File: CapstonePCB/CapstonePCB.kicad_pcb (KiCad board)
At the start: 2 copper layers, 42 parts, among them J1 Conn_02x40_Counter_Clockwise, J2 Barrel_Jack, SW1 SW_Push, SW2 SW_Push, SW3 SW_Push, U1 NUCLEO64-F411RE, U2 LP-MSPM0G3507, U3 STSPIN220, U4 SN74AHC14N, U5 LM7805_TO220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

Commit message: Formatting
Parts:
- moved C_EN1 58.1 mm to (194.6, 93.2)
- moved R_COFF1 58.1 mm to (199.0, 91.5)
- moved R_OFF1 58.1 mm to (199.0, 93.2)
- moved R_SNSA1 58.1 mm to (188.9, 82.1)
- moved R_SNSB1 58.1 mm to (196.8, 87.8)
- moved R_STBY1 58.1 mm to (199.0, 78.0)
- moved U3 58.1 mm to (192.8, 84.9)
- moved C_STBY1 58.1 mm to (191.7, 80.5)
- moved R_EN1 58.1 mm to (193.9, 80.5)
- moved C_EN2 58.1 mm to (191.4, 78.0)
- moved C_SPOIL1 58.1 mm to (191.7, 90.7)
- moved C_s1 58.1 mm to (194.3, 88.2)
- moved PullUpResistor2 10.2 mm to (160.0, 104.5), turned to -90 degrees
- moved C3 7.29 mm to (193.0, 27.9)
- moved C_STBY3 2.54 mm to (33.0, 22.8)
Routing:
- net GNDREF: track 189.5 -> 269.6 mm
- net +12V: track 21.0 -> 23.2 mm
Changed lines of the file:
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@@
 	(footprint "Resistor_SMD:R_0201_0603Metric"
 		(layer "F.Cu")
-		(at 243.495 54.13)
+		(at 199.0125 91.4925)
 		(descr "Resistor SMD 0201 (0603 Metric), square (rectangular) end terminal, IPC-7351 nominal, (Body size source: https://www.vishay.com/docs/20052/crcw0201e3.pdf), generated with kicad-footprint-generator")
 		(tags "resistor")
@@
 	(footprint "Capacitor_SMD:C_0201_0603Metric"
 		(layer "F.Cu")
-		(at 235.875 40.64)
+		(at 191.3925 78.0025)
 		(descr "Capacitor SMD 0201 (0603 Metric), square (rectangular) end terminal, IPC-7351 nominal, (Body size source: https://www.vishay.com/docs/20052/crcw0201e3.pdf), generated with kicad-footprint-generator")
 		(tags "capacitor")
@@
 	(footprint "Capacitor_SMD:C_0201_0603Metric"
 		(layer "F.Cu")
-		(at 236.22 43.18)
+		(at 191.7375 80.5425)
 		(descr "Capacitor SMD 0201 (0603 Metric), square (rectangular) end terminal, IPC-7351 nominal, (Body size source: https://www.vishay.com/docs/20052/crcw0201e3.pdf), generated with kicad-footprint-generator")
 		(tags "capacitor")
@@
 	(footprint "Capacitor_SMD:C_0201_0603Metric"
 		(layer "F.Cu")
-		(at 236.22 53.34)
+		(at 191.7375 90.7025)
 		(descr "Capacitor SMD 0201 (0603 Metric), square (rectangular) end terminal, IPC-7351 nominal, (Body size source: https://www.vishay.com/docs/20052/crcw0201e3.pdf), generated with kicad-footprint-generator")
 		(tags "capacitor")
@@
 	(footprint "Resistor_SMD:R_0201_0603Metric"
 		(layer "F.Cu")
-		(at 169.835 101.6)
+		(at 160.02 104.46 -90)
 		(descr "Resistor SMD 0201 (0603 Metric), square (rectangular) end terminal, IPC-7351 nominal, (Body size source: https://www.vishay.com/docs/20052/crcw0201e3.pdf), generated with kicad-footprint-generator")
 		(tags "resistor")
 		(property "Reference" "PullUpResistor2"
-			(at 0 -1.05 0)
+			(at 0 -1.05 90)
 			(layer "F.SilkS")
 			(effects
@@
 		)
 		(property "Value" "10 kOhm"
-			(at 0 1.05 0)
+			(at 0 1.05 90)
 			(layer "F.Fab")
 			(effects
@@
 		)
 		(property "Datasheet" "~"
-			(at 0 0 0)
+			(at 0 0 90)
 			(layer "F.Fab")
 			(hide yes)
@@
 		)
 		(property "Description" "Resistor"
-			(at 0 0 0)
+			(at 0 0 90)
 			(layer "F.Fab")
 			(hide yes)
@@
 		(attr smd)
 		(fp_line
-			(start -0.7 -0.35)
-			(end 0.7 -0.35)
+			(start -0.7 0.35)
+			(end -0.7 -0.35)
 			(stroke
 				(width 0.05)
@@
 		)
 		(fp_line
-			(start -0.7 0.35)
-			(end -0.7 -0.35)
+			(start 0.7 0.35)
+			(end -0.7 0.35)
 			(stroke
 				(width 0.05)
@@
 		)
 		(fp_line
-			(start 0.7 -0.35)
-			(end 0.7 0.35)
+			(start -0.7 -0.35)
+			(end 0.7 -0.35)
 			(stroke
 				(width 0.05)
@@
 		)
 		(fp_line
-			(start 0.7 0.35)
-			(end -0.7 0.35)
+			(start 0.7 -0.35)
+			(end 0.7 0.35)
 			(stroke
 				(width 0.05)
@@
 		)
 		(fp_line
-			(start -0.3 -0.15)
-			(end 0.3 -0.15)
+			(start -0.3 0.15)
+			(end -0.3 -0.15)
 			(stroke
 				(width 0.1)
@@
 		)
 		(fp_line
-			(start -0.3 0.15)
-			(end -0.3 -0.15)
+			(start 0.3 0.15)
+			(end -0.3 0.15)
 			(stroke
 				(width 0.1)
@@
 		)
 		(fp_line
-			(start 0.3 -0.15)
-			(end 0.3 0.15)
+			(start -0.3 -0.15)
+			(end 0.3 -0.15)
 			(stroke
 				(width 0.1)
@@
 		)
 		(fp_line
-			(start 0.3 0.15)
-			(end -0.3 0.15)
+			(start 0.3 -0.15)
+			(end 0.3 0.15)
 			(stroke
 				(width 0.1)
@@
 		)
 		(fp_text user "${REFERENCE}"
-			(at 0 -0.68 0)
+			(at 0 -0.68 90)
 			(layer "F.Fab")
 			(effects
@@
 		)
 		(pad "" smd roundrect
-			(at -0.345 0)
+			(at -0.345 0 270)
 			(size 0.318 0.36)
 			(layers "F.Paste")
@@
 		)
 		(pad "" smd roundrect
-			(at 0.345 0)
+			(at 0.345 0 270)
 			(size 0.318 0.36)
 			(layers "F.Paste")
@@
 		)
 		(pad "1" smd roundrect
-			(at -0.32 0)
+			(at -0.32 0 270)
 			(size 0.46 0.4)
 			(layers "F.Cu" "F.Mask")
@@
 		)
 		(pad "2" smd roundrect
-			(at 0.32 0)
+			(at 0.32 0 270)
 			(size 0.46 0.4)
 			(layers "F.Cu" "F.Mask")
@@
 	(footprint "Resistor_SMD:R_0201_0603Metric"
 		(layer "F.Cu")
-		(at 241.3 50.48 -90)
+		(at 196.8175 87.8425 -90)
 		(descr "Resistor SMD 0201 (0603 Metric), square (rectangular) end terminal, IPC-7351 nominal, (Body size source: https://www.vishay.com/docs/20052/crcw0201e3.pdf), generated with kicad-footprint-generator")
 		(tags "resistor")
@@
 	(footprint "Resistor_SMD:R_0201_0603Metric"
 		(layer "F.Cu")
-		(at 243.495 55.88)
+		(at 199.0125 93.2425)
 		(descr "Resistor SMD 0201 (0603 Metric), square (rectangular) end terminal, IPC-7351 nominal, (Body size source: https://www.vishay.com/docs/20052/crcw0201e3.pdf), generated with kicad-footprint-generator")
 		(tags "resistor")
@@
 	(footprint "Capacitor_THT:C_Radial_D10.0mm_H20.0mm_P5.00mm"
 		(layer "F.Cu")
-		(at 30.48 22.78 90)
+		(at 33.02 22.78 90)
 		(descr "C, Radial series, Radial, pin pitch=5.00mm, diameter=10mm, height=20mm, Non-Polar Electrolytic Capacitor")
 		(tags "C Radial series Radial pin pitch 5.00mm diameter 10mm height 20mm Non-Polar Electrolytic Capacitor")
@@
 	(footprint "Capacitor_SMD:C_0201_0603Metric"
 		(layer "F.Cu")
-		(at 238.76 50.8)
+		(at 194.2775 88.1625)
 		(descr "Capacitor SMD 0201 (0603 Metric), square (rectangular) end terminal, IPC-7351 nominal, (Body size source: https://www.vishay.com/docs/20052/crcw0201e3.pdf), generated with kicad-footprint-generator")
 		(tags "capacitor")
@@
 	(footprint "Package_DFN_QFN:VQFN-16-1EP_3x3mm_P0.5mm_EP1.8x1.8mm"
 		(layer "F.Cu")
-		(at 237.2725 47.51)
+		(at 192.79 84.8725)
 		(descr "VQFN, 16 Pin (https://www.st.com/resource/en/datasheet/stspin220.pdf), generated with kicad-footprint-generator ipc_noLead_generator.py")
 		(tags "VQFN NoLead")
@@
 	(footprint "Capacitor_SMD:C_0201_0603Metric"
 		(layer "F.Cu")
-		(at 192.695 35.22)
+		(at 193.04 27.94)
 		(descr "Capacitor SMD 0201 (0603 Metric), square (rectangular) end terminal, IPC-7351 nominal, (Body size source: https://www.vishay.com/docs/20052/crcw0201e3.pdf), generated with kicad-footprint-generator")
 		(tags "capacitor")
@@
 	(footprint "Capacitor_SMD:C_0201_0603Metric"
 		(layer "F.Cu")
-		(at 239.08 55.88 180)
+		(at 194.5975 93.2425 180)
 		(descr "Capacitor SMD 0201 (0603 Metric), square (rectangular) end terminal, IPC-7351 nominal, (Body size source: https://www.vishay.com/docs/20052/crcw0201e3.pdf), generated with kicad-footprint-generator")
 		(tags "capacitor")
@@
 	(footprint "Resistor_SMD:R_0201_0603Metric"
 		(layer "F.Cu")
-		(at 233.335 44.76)
+		(at 188.8525 82.1225)
 		(descr "Resistor SMD 0201 (0603 Metric), square (rectangular) end terminal, IPC-7351 nominal, (Body size source: https://www.vishay.com/docs/20052/crcw0201e3.pdf), generated with kicad-footprint-generator")
 		(tags "resistor")
@@
 	(footprint "Resistor_SMD:R_0201_0603Metric"
 		(layer "F.Cu")
-		(at 243.495 40.64)
+		(at 199.0125 78.0025)
 		(descr "Resistor SMD 0201 (0603 Metric), square (rectangular) end terminal, IPC-7351 nominal, (Body size source: https://www.vishay.com/docs/20052/crcw0201e3.pdf), generated with kicad-footprint-generator")
 		(tags "resistor")
@@
 	(footprint "Resistor_SMD:R_0201_0603Metric"
 		(layer "F.Cu")
-		(at 238.415 43.18)
+		(at 193.9325 80.5425)
 		(descr "Resistor SMD 0201 (0603 Metric), square (rectangular) end terminal, IPC-7351 nominal, (Body size source: https://www.vishay.com/docs/20052/crcw0201e3.pdf), generated with kicad-footprint-generator")
 		(tags "resistor")
@@
 	)
 	(segment
-		(start 30.48 24.45)
-		(end 34.895 28.865)
+		(start 27.94 26.99)
+		(end 28.81 26.99)
+		(width 0.25)
+		(layer "F.Cu")
+		(net 168)
+	)
+	(segment
+		(start 33.02 22.78)
+		(end 33.02 26.99)
 		(width 0.25)
 		(layer "F.Cu")
@@
 	)
 	(segment
-		(start 30.48 24.45)
-		(end 27.94 26.99)
+		(start 28.81 26.99)
+		(end 33.02 22.78)
 		(width 0.25)
 		(layer "F.Cu")
@@
 	)
 	(segment
-		(start 30.48 22.78)
-		(end 30.48 24.45)
+		(start 34.895 28.865)
+		(end 34.895 30.48)
 		(width 0.25)
 		(layer "F.Cu")
@@
 	)
 	(segment
-		(start 34.895 28.865)
-		(end 34.895 30.48)
+		(start 33.02 26.99)
+		(end 34.895 28.865)
 		(width 0.25)
 		(layer "F.Cu")
@@
 	)
 	(segment
+		(start 147.020884 94.074)
+		(end 154.034 94.074)
+		(width 0.25)
+		(layer "F.Cu")
+		(net 169)
+	)
+	(segment
 		(start 22.86 33.97)
 		(end 22.86 38.1)
@@
 	)
 	(segment
+		(start 145.562884 92.616)
+		(end 147.020884 94.074)
+		(width 0.25)
+		(layer "F.Cu")
+		(net 169)
+	)
+	(segment
 		(start 84.906 143.326)
 		(end 83.82 142.24)
@@
 	)
 	(segment
+		(start 22.86 17.78)
+		(end 33.02 17.78)
+		(width 0.25)
+		(layer "F.Cu")
+		(net 169)
+	)
+	(segment
+		(start 87.536 92.616)
+		(end 145.562884 92.616)
+		(width 0.25)
+		(layer "F.Cu")
+		(net 169)
+	)
+	(segment
 		(start 35.56 35.56)
 		(end 35.56 39.951116)
@@
 	)
 	(segment
+		(start 87.446 92.526)
+		(end 87.536 92.616)
+		(width 0.25)
+		(layer "F.Cu")
+		(net 169)
+	)
+	(segment
 		(start 28.89 28.89)
 		(end 35.56 35.56)
@@
 	)
 	(segment
+		(start 156.77 96.81)
+		(end 163.27 96.81)
+		(width 0.25)
+		(layer "F.Cu")
+		(net 169)
+	)
+	(segment
 		(start 20.32 20.32)
 		(end 17.696 22.944)
@@
 	)
 	(segment
-		(start 30.48 17.78)
-		(end 22.86 17.78)
-		(width 0.25)
-		(layer "F.Cu")
-		(net 169)
-	)
-	(segment
 		(start 46.207116 49.624)
 		(end 46.896 50.312884)
@@
 		(width 0.25)
 		(layer "F.Cu")
+		(net 169)
+	)
+	(segment
+		(start 154.034 94.074)
+		(end 156.77 96.81)
+		(width 0.25)
+		(layer "F.Cu")

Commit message: Updated button routing
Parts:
- CSW1: renamed from C1; value 0.47 uF -> 0.47uF
- CSW3: renamed from C2; value 0.47 uF -> 0.47uF
- PullUpResistorSW1: renamed from PullUpResistor1; value 10 kOhm -> 10kOhm
- PullUpResistorSW3: renamed from PullUpResistor3; value 10 kOhm -> 10kOhm
- RSW1: renamed from R1; value 10 kOhm -> 10kOhm
- moved U7 86.1 mm to (256.5, 69.5)
- moved PullUpResistorJS1 54.3 mm to (246.0, 50.8)
- moved CJS1 51.1 mm to (235.9, 55.9)
- moved RJS1 43.4 mm to (235.9, 48.3)
- moved PullUpResistorSW3 30.1 mm to (221.7, 30.8)
- moved RSW3 12.2 mm to (201.0, 33.3)
- moved SW1 11.4 mm to (205.0, 18.1)
- moved CSW3 10.5 mm to (201.1, 28.2)
- moved SW3 10.5 mm to (207.6, 28.2)
- moved CSW1 10.2 mm to (200.7, 17.8)
- moved RSW1 7.83 mm to (200.3, 22.9), turned to 0 degrees
- moved PullUpResistorSW1 7.43 mm to (218.4, 20.0)
- renumbered C3 to CJS1, PullUpResistor4 to PullUpResistorJS1, R3 to RJS1, R2 to RSW3
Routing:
- net +5V: track 136.0 -> 324.0 mm
- net GNDREF: track 269.6 -> 358.7 mm
- net Net-(J1-Pin_5): track 2.54 -> 36.4 mm
- net Net-(J1-Pin_3): track 2.54 -> 35.3 mm
- net Net-(J1-Pin_1): track 2.54 -> 34.3 mm
- net Net-(U4-2A): track 0.00 -> 28.0 mm
- net Net-(U4-1A): track 0.00 -> 25.5 mm
- net VDD: track 243.0 -> 219.3 mm
- net /Button2 Input: track 0.00 -> 21.1 mm
- net /Button1 Input: track 0.00 -> 18.9 mm
- net /Button No Debouning: track 2.54 -> 18.7 mm

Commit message: Updated rounting
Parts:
- renumbered C_STBY2 to C_BP1, C_STBY3 to C_BP2
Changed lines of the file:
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@@
 		(descr "Capacitor SMD 0805 (2012 Metric), square (rectangular) end terminal, IPC-7351 nominal, (Body size source: IPC-SM-782 page 76, https://www.pcb-3d.com/wordpress/wp-content/uploads/ipc-sm-782a_amendment_1_and_2.pdf, https://docs.google.com/spreadsheets/d/1BsfQQcO9C6DZCsRaXUlFlo91Tg2WpOkGARC1WS5S8t0/edit?usp=sharing), generated with kicad-footprint-generator")
 		(tags "capacitor")
-		(property "Reference" "C_STBY2"
+		(property "Reference" "C_BP1"
 			(at 0 -1.68 90)
 			(layer "F.SilkS")
@@
 		(descr "C, Radial series, Radial, pin pitch=5.00mm, diameter=10mm, height=20mm, Non-Polar Electrolytic Capacitor")
 		(tags "C Radial series Radial pin pitch 5.00mm diameter 10mm height 20mm Non-Polar Electrolytic Capacitor")
-		(property "Reference" "C_STBY3"
+		(property "Reference" "C_BP2"
 			(at 2.5 -6.25 90)
 			(layer "F.SilkS")

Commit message: Formatting change
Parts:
- moved U8 1.95 mm to (165.1, 114.3)
- renumbered R_STBY2 to R_INDC1
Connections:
- J1 pad 27: GNDREF -> Net-(J1-Pin_27)
- J1 pad 28: GNDREF -> Net-(J1-Pin_27)
- U3 pad 11: GNDREF -> unconnected-(U3-REF-Pad11)
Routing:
- net GNDREF: track 358.7 -> 27.2 mm
- net +5V: track 324.0 -> 287.4 mm
- net VDD: track 219.3 -> 196.9 mm
- net Net-(J1-Pin_79): track 2.54 -> 21.3 mm
- net Net-(J1-Pin_77): track 2.54 -> 21.1 mm
- net +12V: track 23.2 -> 35.0 mm
- net Net-(J1-Pin_27): track 0.00 -> 2.54 mm

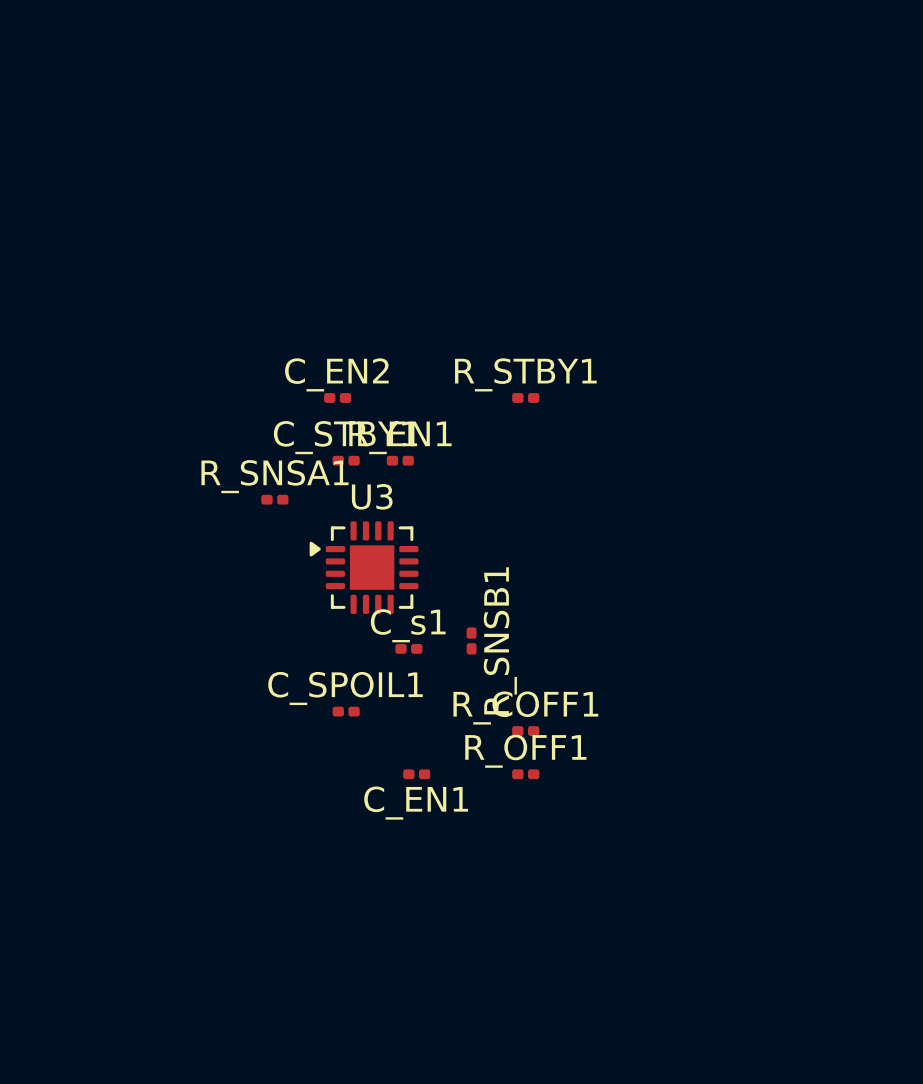
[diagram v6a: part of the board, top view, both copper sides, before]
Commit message: Changed caps to through-hole
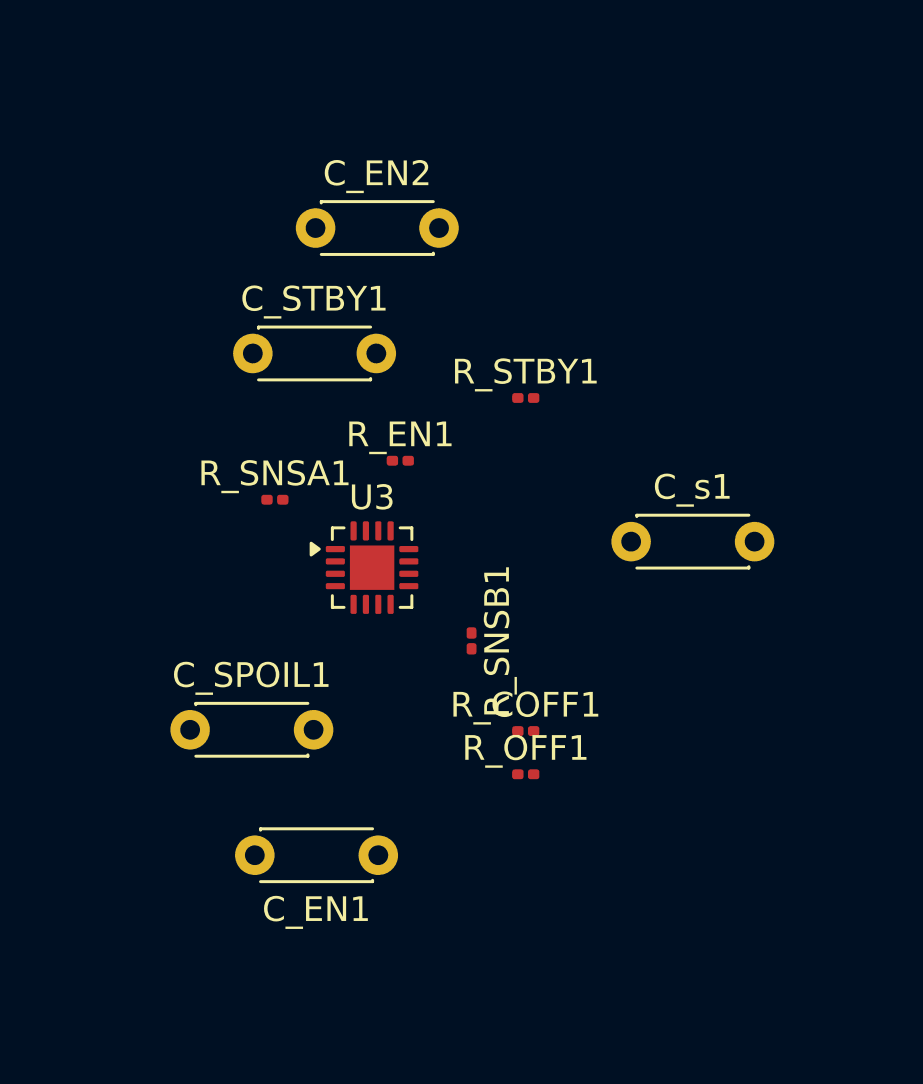
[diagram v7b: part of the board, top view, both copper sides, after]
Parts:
- C_EN1, C_EN2, C_SPOIL1, C_STBY1, C_s1: footprint Capacitor_SMD:C_0201_0603Metric -> Capacitor_THT:C_Disc_D4.3mm_W1.9mm_P5.00mm
- moved C_s1 10.00 mm to (203.3, 83.8)
- moved C_EN2 6.94 mm to (190.5, 71.1)
- moved C_SPOIL1 6.36 mm to (185.4, 91.4)
- moved C_STBY1 5.76 mm to (188.0, 76.2)
- moved C_EN1 3.63 mm to (193.0, 96.5)
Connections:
- U3 pad 11: unconnected-(U3-REF-Pad11) -> Net-(J1-Pin_27)
- U7 pad H2: Net-(J1-Pin_21) -> Net-(J1-Pin_11)
- U7 pad V2: Net-(J1-Pin_23) -> Net-(J1-Pin_13)

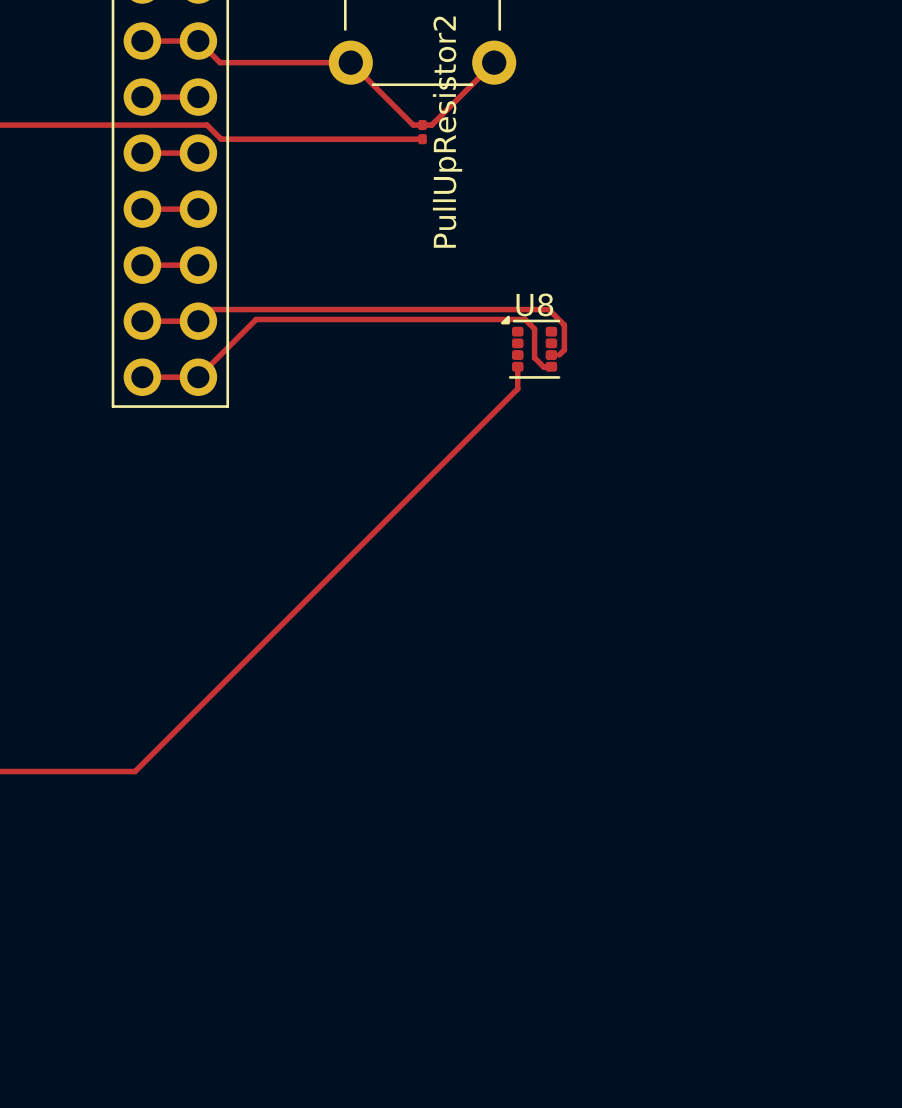
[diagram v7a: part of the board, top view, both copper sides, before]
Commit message: Added LCD connector to schematic
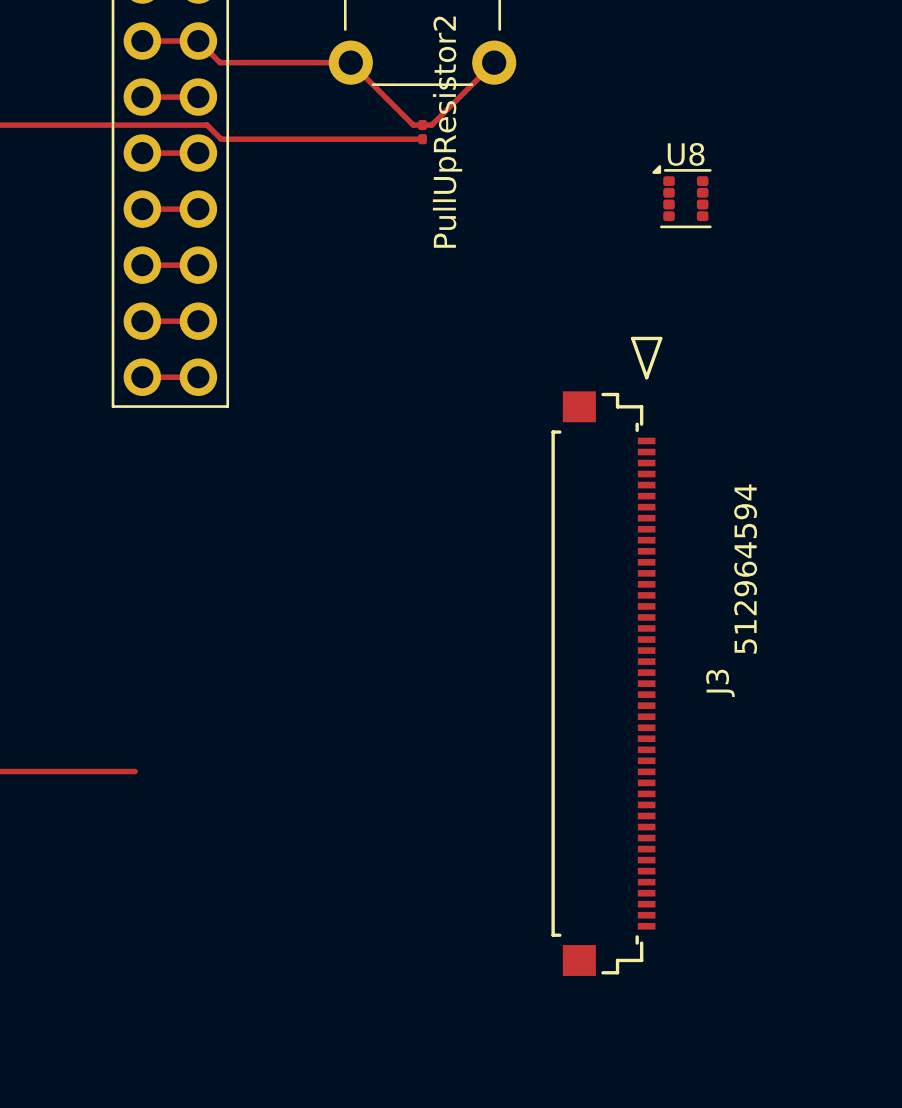
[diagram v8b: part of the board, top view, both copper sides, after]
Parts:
- added J3: 512964594, CorrectlLCDconnector:CON_512964594_MOL, F.Cu at (168.1, 129.5)
- moved U8 9.68 mm to (172.0, 107.5)
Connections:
- J1 pad 63: Net-(J1-Pin_63) -> /Button No Debouning
- J1 pad 64: Net-(J1-Pin_63) -> /Button No Debouning
- J1 pad 67: /Button No Debouning -> Net-(J1-Pin_67)
- J1 pad 68: /Button No Debouning -> Net-(J1-Pin_67)
- U8 pad 5: Net-(J1-Pin_79) -> unconnected-(U8-SCL-Pad5)
- U8 pad 6: Net-(J1-Pin_77) -> unconnected-(U8-SDA-Pad6)
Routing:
- net VDD: track 196.9 -> 171.4 mm
- net Net-(J1-Pin_79): track 21.3 -> 2.54 mm
- net Net-(J1-Pin_77): track 21.1 -> 3.29 mm
- net Net-(J1-Pin_63): track 2.54 -> 0.00 mm
- net /Button No Debouning: track 18.7 -> 21.2 mm
